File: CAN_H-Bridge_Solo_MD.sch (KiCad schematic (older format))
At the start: 49 parts, among them IC1 SI8650AB-B-IS1, IC2 A3921KLPTR-T, IC3 AP7381-50SA-7, J2 Conn_01x03, J3 Conthrough, J4 Bus_mechaken_PCIexpress_x16_1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, M1 Motor_DC, Q1 IRFB3806PBF, Q2 IRFB3806PBF, Q3 IRFB3806PBF, Q4 IRFB3806PBF, U1 LDL1117S33R_SOT223-4, U2 STM32F042K6Tx, U3 MCP2562-E-SN, U4 LDL1117S33TR_SOT223-4

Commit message: change
反転前
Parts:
- removed C14: 2.2u, Capacitor_SMD:C_0805_2012Metric_Pad1.15x1.40mm_HandSolder, symbol Device:C
- removed C15: 1u, Capacitor_SMD:C_0805_2012Metric_Pad1.15x1.40mm_HandSolder, symbol Device:C
- removed IC3: AP7381-50SA-7, SamacSys_Parts:SOT96P240X105-3N, symbol CAN_H-Bridge_Solo_MD-rescue:AP7381-50SA-7-SamacSys_Parts
- removed Q1, Q2, Q3, Q4: IRFB3806PBF, Package_TO_SOT_THT:TO-220-3_Vertical, symbol Transistor_FET:IRLB8721PBF
- added Q1, Q2, Q3, Q4: TK6R7P06PLRQ, Package_TO_SOT_SMD:TO-252-2, symbol Device:Q_NMOS_GDS
- C7: renamed from C13; value 4.7uF -> 1uF
- S1: value IKD0403101 -> DIPSW; footprint SamacSys_Parts:SOP254P980X370-8N -> Package_DIP:DIP-8_W7.62mm; symbol SamacSys_Parts:IKD0403101 -> Switch:SW_DIP_x04; Description 4 Way Surface Mount DIP Switch SPST, Raised Actuator Slide 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 -> (none)
- U1: symbol H-Bridge-MD-rescue:LD1117S33TR_SOT223-Regulator_Linear -> Regulator_Linear:LD1117S33TR_SOT223
- U2: value STM32F042K6Tx -> STM32F303K8
- U3: renamed from U4; value LDL1117S33TR_SOT223-4 -> MCP1799T-3302H/TT; footprint Package_TO_SOT_SMD:SOT-223-3_TabPin2 -> Package_TO_SOT_SMD:SOT-23; symbol H-Bridge-MD-rescue:LD1117S33TR_SOT223-Regulator_Linear -> Regulator_Linear:MCP1700-3302E_SOT23
- renumbered C3 to C1, C7 to C10, C6 to C11, C8 to C12, C12 to C13, C9 to C14, C10 to C15, C1 to C2, C2 to C3, C11 to C6, C5 to C8, C4 to C9, D6 to D1, D1 to D2, D2 to D3, D3 to D4, D4 to D5, D5 to D6, IC1 to IC2, IC2 to IC3, J2 to J1, J3 to J2, J4 to J3, R5 to R1, R8 to R10, R4 to R11, R9 to R12, R1 to R2, R2 to R3, R10 to R4, R11 to R5, R12 to R6, R6 to R7, R7 to R8, R3 to R9, U3 to U4
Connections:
- net labels added: IC_3V3
- net labels removed: +3.3V
- wire segments 114 -> 107
- no-connect marks 20 -> 19

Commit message: change
FET反転
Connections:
- net SA_0: now also M1.1 (+); no longer M1.2 (-)
- net SB_0: now also M1.2 (-); no longer M1.1 (+)
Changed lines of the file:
@@
 L Motor:Motor_DC M1
 U 1 1 5E054D53
-P 3550 6700
-F 0 "M1" V 3845 6650 50  0000 C CNN
-F 1 "Motor_DC" V 3754 6650 50  0000 C CNN
-F 2 "XT60:XT60PW" H 3550 6610 50  0001 C CNN
-F 3 "~" H 3550 6610 50  0001 C CNN
-	1    3550 6700
-	0    1    1    0
+P 3450 6700
+F 0 "M1" V 3745 6650 50  0000 C CNN
+F 1 "Motor_DC" V 3654 6650 50  0000 C CNN
+F 2 "XT60:XT60PW" H 3450 6610 50  0001 C CNN
+F 3 "~" H 3450 6610 50  0001 C CNN
+	1    3450 6700
+	0    -1   -1   0
 $EndComp
 Wire Wire Line

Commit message: change
ビアなどの増加
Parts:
- IC2: symbol SamacSys_Parts:SI8650AB-B-IS1 -> CAN_H-Bridge_Solo_MD-rescue:SI8650AB-B-IS1-SamacSys_Parts
- IC3: symbol SamacSys_Parts:A3921KLPTR-T -> CAN_H-Bridge_Solo_MD-rescue:A3921KLPTR-T-SamacSys_Parts
- U1: value LDL1117S33R_SOT223-4 -> AP2210N-3.3TRG1; footprint Package_TO_SOT_SMD:SOT-223-3_TabPin2 -> Package_TO_SOT_SMD:SOT-23
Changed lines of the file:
@@
 NoConn ~ 7800 5750
 $Comp
-L SamacSys_Parts:A3921KLPTR-T IC3
+L CAN_H-Bridge_Solo_MD-rescue:A3921KLPTR-T-SamacSys_Parts IC3
 U 1 1 5DC023BF
 P 7800 4450
@@
 Wire Wire Line
 	5450 3000 5450 3300
-$Comp
-L Regulator_Linear:LD1117S33TR_SOT223 U1
-U 1 1 5DEBD597
-P 1350 1950
-F 0 "U1" H 1200 2075 50  0000 C CNN
-F 1 "LDL1117S33R_SOT223-4" H 1350 2075 50  0000 L CNN
-F 2 "Package_TO_SOT_SMD:SOT-223-3_TabPin2" H 1350 2150 50  0001 C CNN
-F 3 "http://www.st.com/st-web-ui/static/active/en/resource/technical/document/datasheet/CD00000544.pdf" H 1450 1700 50  0001 C CNN
-	1    1350 1950
-	1    0    0    -1
-$EndComp
 $Comp
 L power:+5V #PWR01
@@
 IC_3V3
 $Comp
-L SamacSys_Parts:SI8650AB-B-IS1 IC2
+L CAN_H-Bridge_Solo_MD-rescue:SI8650AB-B-IS1-SamacSys_Parts IC2
 U 1 1 5DC0259A
 P 7250 3050
@@
 Wire Wire Line
 	5900 1350 5900 1450
+$Comp
+L Regulator_Linear:LD1117S33TR_SOT223 U1
+U 1 1 5DEBD597
+P 1350 1950
+F 0 "U1" H 1200 2075 50  0000 C CNN
+F 1 "AP2210N-3.3TRG1" H 1350 2075 50  0000 L CNN
+F 2 "Package_TO_SOT_SMD:SOT-23" H 1350 2150 50  0001 C CNN
+F 3 "" H 1450 1700 50  0001 C CNN
+	1    1350 1950
+	1    0    0    -1
+$EndComp
 $EndSCHEMATC

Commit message: Release
Release Prototype-2.0
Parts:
- C1, C13, C14, C8, C9: value 0.1uF -> 0.1u
- C10, C11, C12: value 4.7uF -> 4.7u
- C15: value 0.47uF -> 0.47u
- C2, C6, C7: value 1uF -> 1u
- C3: value 4.7uF -> 2.2u
- IC2: footprint SamacSys_Parts:SOIC127P600X175-16N -> Package_SO:SOIC-16_3.9x9.9mm_P1.27mm; symbol CAN_H-Bridge_Solo_MD-rescue:SI8650AB-B-IS1-SamacSys_Parts -> SamacSys_Parts:SI8650AB-B-IS1
- IC3: symbol CAN_H-Bridge_Solo_MD-rescue:A3921KLPTR-T-SamacSys_Parts -> SamacSys_Parts:A3921KLPTR-T
- R10, R11, R12, R9: value 21 -> 30
- U1: footprint Package_TO_SOT_SMD:SOT-23 -> Package_TO_SOT_SMD:SOT-23W_Handsoldering
- U3: footprint Package_TO_SOT_SMD:SOT-23 -> Package_TO_SOT_SMD:SOT-23_Handsoldering
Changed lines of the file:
@@
 P 9900 5400
 F 0 "C13" H 10015 5446 50  0000 L CNN
-F 1 "0.1uF" H 10015 5355 50  0000 L CNN
+F 1 "0.1u" H 10015 5355 50  0000 L CNN
 F 2 "Capacitor_SMD:C_0805_2012Metric_Pad1.15x1.40mm_HandSolder" H 9938 5250 50  0001 C CNN
 F 3 "~" H 9900 5400 50  0001 C CNN
@@
 P 7450 5800
 F 0 "C14" H 7565 5846 50  0000 L CNN
-F 1 "0.1uF" H 7565 5755 50  0000 L CNN
+F 1 "0.1u" H 7565 5755 50  0000 L CNN
 F 2 "Capacitor_SMD:C_0805_2012Metric_Pad1.15x1.40mm_HandSolder" H 7488 5650 50  0001 C CNN
 F 3 "~" H 7450 5800 50  0001 C CNN
@@
 NoConn ~ 7800 5750
 $Comp
-L CAN_H-Bridge_Solo_MD-rescue:A3921KLPTR-T-SamacSys_Parts IC3
+L SamacSys_Parts:A3921KLPTR-T IC3
 U 1 1 5DC023BF
 P 7800 4450
@@
 P 5900 3950
 F 0 "C8" V 5648 3950 50  0000 C CNN
-F 1 "0.1uF" V 5739 3950 50  0000 C CNN
+F 1 "0.1u" V 5739 3950 50  0000 C CNN
 F 2 "Capacitor_SMD:C_0805_2012Metric_Pad1.15x1.40mm_HandSolder" H 5938 3800 50  0001 C CNN
 F 3 "~" H 5900 3950 50  0001 C CNN
@@
 P 4500 4600
 F 0 "C9" V 4248 4600 50  0000 C CNN
-F 1 "0.1uF" V 4339 4600 50  0000 C CNN
+F 1 "0.1u" V 4339 4600 50  0000 C CNN
 F 2 "Capacitor_SMD:C_0805_2012Metric_Pad1.15x1.40mm_HandSolder" H 4538 4450 50  0001 C CNN
 F 3 "~" H 4500 4600 50  0001 C CNN
@@
 P 1000 2100
 F 0 "C2" V 748 2100 50  0000 C CNN
-F 1 "1uF" V 839 2100 50  0000 C CNN
+F 1 "1u" V 839 2100 50  0000 C CNN
 F 2 "Capacitor_SMD:C_0805_2012Metric_Pad1.15x1.40mm_HandSolder" H 1038 1950 50  0001 C CNN
 F 3 "~" H 1000 2100 50  0001 C CNN
@@
 P 1700 2100
 F 0 "C3" V 1448 2100 50  0000 C CNN
-F 1 "4.7uF" V 1539 2100 50  0000 C CNN
+F 1 "2.2u" V 1539 2100 50  0000 C CNN
 F 2 "Capacitor_SMD:C_0805_2012Metric_Pad1.15x1.40mm_HandSolder" H 1738 1950 50  0001 C CNN
 F 3 "~" H 1700 2100 50  0001 C CNN
@@
 P 4100 1150
 F 0 "C1" V 3848 1150 50  0000 C CNN
-F 1 "0.1uF" V 3939 1150 50  0000 C CNN
+F 1 "0.1u" V 3939 1150 50  0000 C CNN
 F 2 "Capacitor_SMD:C_0805_2012Metric_Pad1.15x1.40mm_HandSolder" H 4138 1000 50  0001 C CNN
 F 3 "~" H 4100 1150 50  0001 C CNN
@@
 P 7150 4900
 F 0 "C10" H 7264 4854 50  0000 L CNN
-F 1 "4.7uF" H 7264 4945 50  0000 L CNN
+F 1 "4.7u" H 7264 4945 50  0000 L CNN
 F 2 "Capacitor_SMD:C_0805_2012Metric_Pad1.15x1.40mm_HandSolder" H 7188 4750 50  0001 C CNN
 F 3 "~" H 7150 4900 50  0001 C CNN
@@
 P 7150 5400
 F 0 "C12" H 6823 5446 50  0000 L CNN
-F 1 "4.7uF" H 6823 5355 50  0000 L CNN
+F 1 "4.7u" H 6823 5355 50  0000 L CNN
 F 2 "Capacitor_SMD:C_0805_2012Metric_Pad1.15x1.40mm_HandSolder" H 7188 5250 50  0001 C CNN
 F 3 "~" H 7150 5400 50  0001 C CNN
@@
 P 9450 5800
 F 0 "C15" H 9074 5754 50  0000 L CNN
-F 1 "0.47uF" H 9074 5845 50  0000 L CNN
+F 1 "0.47u" H 9074 5845 50  0000 L CNN
 F 2 "Capacitor_SMD:C_0805_2012Metric_Pad1.15x1.40mm_HandSolder" H 9488 5650 50  0001 C CNN
 F 3 "~" H 9450 5800 50  0001 C CNN
@@
 P 6300 5000
 F 0 "C11" H 6415 5046 50  0000 L CNN
-F 1 "4.7uF" H 6415 4955 50  0000 L CNN
+F 1 "4.7u" H 6415 4955 50  0000 L CNN
 F 2 "Capacitor_SMD:C_0805_2012Metric_Pad1.15x1.40mm_HandSolder" H 6338 4850 50  0001 C CNN
 F 3 "~" H 6300 5000 50  0001 C CNN
@@
 P 9900 3150
 F 0 "C6" V 9648 3150 50  0000 C CNN
-F 1 "1uF" V 9739 3150 50  0000 C CNN
+F 1 "1u" V 9739 3150 50  0000 C CNN
 F 2 "Capacitor_SMD:C_0805_2012Metric_Pad1.15x1.40mm_HandSolder" H 9938 3000 50  0001 C CNN
 F 3 "~" H 9900 3150 50  0001 C CNN
@@
 P 10600 3150
 F 0 "C7" V 10348 3150 50  0000 C CNN
-F 1 "1uF" V 10439 3150 50  0000 C CNN
+F 1 "1u" V 10439 3150 50  0000 C CNN
 F 2 "Capacitor_SMD:C_0805_2012Metric_Pad1.15x1.40mm_HandSolder" H 10638 3000 50  0001 C CNN
 F 3 "~" H 10600 3150 50  0001 C CNN
@@
 F 0 "U3" H 10100 3125 50  0000 C CNN
 F 1 "MCP1799T-3302H/TT" H 10250 3125 50  0000 L CNN
-F 2 "Package_TO_SOT_SMD:SOT-23" H 10250 3200 50  0001 C CNN
+F 2 "Package_TO_SOT_SMD:SOT-23_Handsoldering" H 10250 3200 50  0001 C CNN
 F 3 "" H 10350 2750 50  0001 C CNN
 	1    10250 3000
@@
 P 4700 7050
 F 0 "R12" V 4815 6975 50  0000 L CNN
-F 1 "21" V 4906 6975 50  0000 L CNN
+F 1 "30" V 4906 6975 50  0000 L CNN
 F 2 "Resistor_SMD:R_0603_1608Metric_Pad1.05x0.95mm_HandSolder" V 4630 7050 50  0001 C CNN
 F 3 "~" H 4700 7050 50  0001 C CNN
@@
 P 2350 6350
 F 0 "R9" V 2550 6275 50  0000 L CNN
-F 1 "21" V 2450 6275 50  0000 L CNN
+F 1 "30" V 2450 6275 50  0000 L CNN
 F 2 "Resistor_SMD:R_0603_1608Metric_Pad1.05x0.95mm_HandSolder" V 2280 6350 50  0001 C CNN
 F 3 "~" H 2350 6350 50  0001 C CNN
@@
 P 2350 7050
 F 0 "R11" V 2550 6974 50  0000 L CNN
-F 1 "21" V 2450 6974 50  0000 L CNN
+F 1 "30" V 2450 6974 50  0000 L CNN
 F 2 "Resistor_SMD:R_0603_1608Metric_Pad1.05x0.95mm_HandSolder" V 2280 7050 50  0001 C CNN
 F 3 "~" H 2350 7050 50  0001 C CNN
@@
 P 4700 6350
 F 0 "R10" V 4815 6276 50  0000 L CNN
-F 1 "21" V 4906 6276 50  0000 L CNN
+F 1 "30" V 4906 6276 50  0000 L CNN
 F 2 "Resistor_SMD:R_0603_1608Metric_Pad1.05x0.95mm_HandSolder" V 4630 6350 50  0001 C CNN
 F 3 "~" H 4700 6350 50  0001 C CNN
@@
 IC_3V3
 $Comp
-L CAN_H-Bridge_Solo_MD-rescue:SI8650AB-B-IS1-SamacSys_Parts IC2
+L SamacSys_Parts:SI8650AB-B-IS1 IC2
 U 1 1 5DC0259A
 P 7250 3050
 F 0 "IC2" H 7473 3315 50  0000 L CNN
 F 1 "SI8650AB-B-IS1" H 7473 3224 50  0000 L CNN
-F 2 "SamacSys_Parts:SOIC127P600X175-16N" H 8200 3150 50  0001 L CNN
+F 2 "Package_SO:SOIC-16_3.9x9.9mm_P1.27mm" H 8200 3150 50  0001 L CNN
 F 3 "https://componentsearchengine.com/Datasheets/1/SI8651BB-B-IS1.pdf" H 8200 3050 50  0001 L CNN
 F 4 "Isolator, Si8650AB-B-IS1 Silicon Labs Si8650AB-B-IS1 PCB SMT 5-channel Digital Isolator, 2.5 kV, 16-Pin SOIC" H 8200 2950 50  0001 L CNN "Description"
@@
 F 0 "U1" H 1200 2075 50  0000 C CNN
 F 1 "AP2210N-3.3TRG1" H 1350 2075 50  0000 L CNN
-F 2 "Package_TO_SOT_SMD:SOT-23" H 1350 2150 50  0001 C CNN
+F 2 "Package_TO_SOT_SMD:SOT-23W_Handsoldering" H 1350 2150 50  0001 C CNN
 F 3 "" H 1450 1700 50  0001 C CNN
 	1    1350 1950

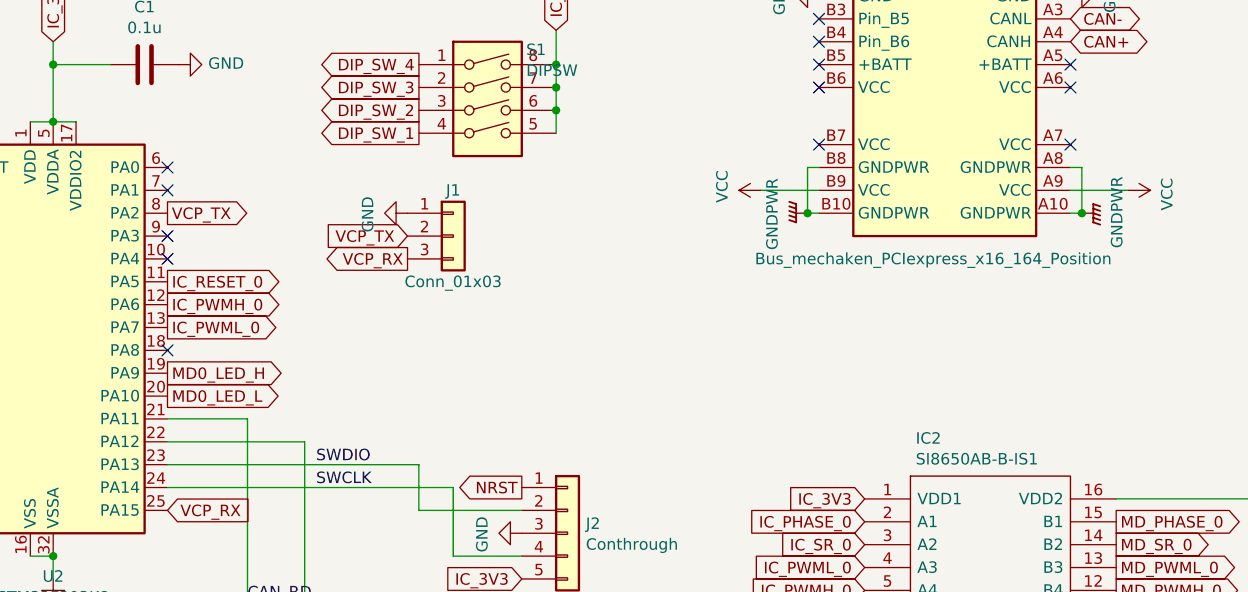
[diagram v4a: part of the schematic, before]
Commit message: Update: エンコーダ対応
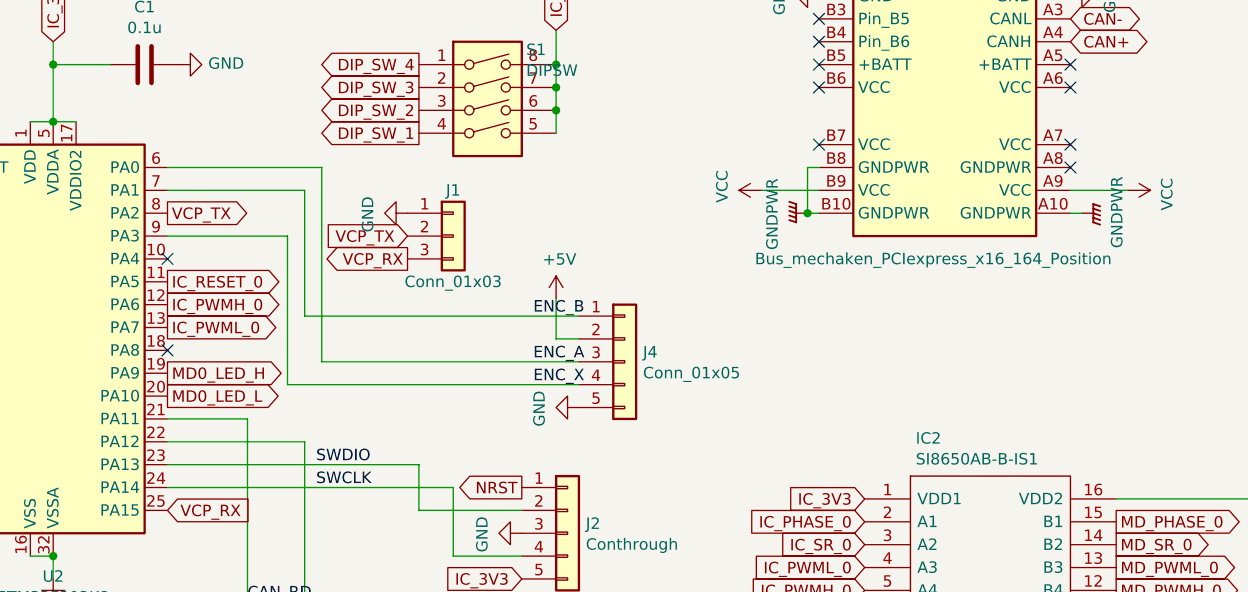
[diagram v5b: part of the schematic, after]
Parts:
- added J4: Conn_01x05, Connector_PinHeader_2.54mm:PinHeader_1x05_P2.54mm_Vertical, symbol Connector_Generic:Conn_01x05
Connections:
- net +5V: now also J4.2 (Pin_2)
- net GND: now also J4.5 (Pin_5)
- net GNDPWR: no longer J3.A8 (GNDPWR)
- net ENC_A: now reaches U2.6 (PA0)
- net ENC_A: now also J4.3 (Pin_3)
- net ENC_B: now reaches U2.7 (PA1)
- net ENC_B: now also J4.1 (Pin_1)
- net ENC_X: now reaches U2.9 (PA3)
- net ENC_X: now also J4.4 (Pin_4)
- no-connect marks 19 -> 17
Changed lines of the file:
@@
 $EndComp
-Wire Wire Line
-	7050 1600 7000 1600
-Wire Wire Line
-	7000 1600 7000 1800
 Wire Wire Line
 	7000 1800 7050 1800
-Connection ~ 7000 1800
 Wire Wire Line
 	7050 1700 6800 1700
 Wire Wire Line
-	8150 1600 8200 1600
-Wire Wire Line
 	8150 1800 8200 1800
 Wire Wire Line
 	8400 1700 8150 1700
-Wire Wire Line
-	8200 1600 8200 1800
-Connection ~ 8200 1800
 NoConn ~ 3200 2100
 NoConn ~ 3200 2200
-NoConn ~ 4200 1600
-NoConn ~ 4200 1700
-NoConn ~ 4200 1900
 NoConn ~ 4200 2000
 NoConn ~ 4200 2400
@@
 	1    0    0    -1
 $EndComp
+$Comp
+L Connector_Generic:Conn_01x05 J4
+U 1 1 602E5899
+P 6200 2450
+F 0 "J4" H 6280 2492 50  0000 L CNN
+F 1 "Conn_01x05" H 6280 2401 50  0000 L CNN
+F 2 "Connector_PinHeader_2.54mm:PinHeader_1x05_P2.54mm_Vertical" H 6200 2450 50  0001 C CNN
+F 3 "~" H 6200 2450 50  0001 C CNN
+	1    6200 2450
+	1    0    0    -1
+$EndComp
+$Comp
+L power:GND #PWR0102
+U 1 1 602E8414
+P 6000 2650
+F 0 "#PWR0102" H 6000 2400 50  0001 C CNN
+F 1 "GND" H 6005 2477 50  0000 C CNN
+F 2 "" H 6000 2650 50  0001 C CNN
+F 3 "" H 6000 2650 50  0001 C CNN
+	1    6000 2650
+	0    1    1    0
+$EndComp
+$Comp
+L power:+5V #PWR0103
+U 1 1 6031EF32
+P 5900 2175
+F 0 "#PWR0103" H 5900 2025 50  0001 C CNN
+F 1 "+5V" H 5915 2348 50  0000 C CNN
+F 2 "" H 5900 2175 50  0001 C CNN
+F 3 "" H 5900 2175 50  0001 C CNN
+	1    5900 2175
+	1    0    0    -1
+$EndComp
+Wire Wire Line
+	5900 2175 5900 2350
+Wire Wire Line
+	5900 2350 6000 2350
+Wire Wire Line
+	4875 1600 4200 1600
+Wire Wire Line
+	4800 1700 4200 1700
+Wire Wire Line
+	4725 2550 4725 1900
+Wire Wire Line
+	4725 1900 4200 1900
+Wire Wire Line
+	4725 2550 6000 2550
+Text Label 5800 2250 0    50   ~ 0
+ENC_B
+Text Label 5800 2450 0    50   ~ 0
+ENC_A
+Text Label 5800 2550 0    50   ~ 0
+ENC_X
+Wire Wire Line
+	4800 1700 4800 2250
+Wire Wire Line
+	4800 2250 6000 2250
+Wire Wire Line
+	4875 1600 4875 2450
+Wire Wire Line
+	4875 2450 6000 2450
+Connection ~ 7000 1800
+Wire Wire Line
+	7000 1600 7000 1800
+Wire Wire Line
+	7050 1600 7000 1600
+NoConn ~ 8150 1600
 $EndSCHEMATC

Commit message: Update: MCUをF042K6からF303K8へ変更
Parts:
- U2: symbol MCU_ST_STM32F0:STM32F042K6Tx -> MCU_ST_STM32F3:STM32F303K8Tx
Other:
- moved on the sheet: R1, U2
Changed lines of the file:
@@
 	-1   0    0    1
 $EndComp
-Text GLabel 3200 1600 0    50   Input ~ 0
+Text GLabel 3100 1600 0    50   Input ~ 0
 NRST
 Text GLabel 4200 3100 2    50   Input ~ 0
@@
 L Device:R R1
 U 1 1 5D5AB267
-P 2650 3100
-F 0 "R1" V 2443 3100 50  0000 C CNN
-F 1 "10k" V 2534 3100 50  0000 C CNN
-F 2 "Resistor_SMD:R_0603_1608Metric_Pad1.05x0.95mm_HandSolder" V 2580 3100 50  0001 C CNN
-F 3 "~" H 2650 3100 50  0001 C CNN
-	1    2650 3100
+P 2550 1800
+F 0 "R1" V 2343 1800 50  0000 C CNN
+F 1 "10k" V 2434 1800 50  0000 C CNN
+F 2 "Resistor_SMD:R_0603_1608Metric_Pad1.05x0.95mm_HandSolder" V 2480 1800 50  0001 C CNN
+F 3 "~" H 2550 1800 50  0001 C CNN
+	1    2550 1800
 	0    1    1    0
 $EndComp
@@
 Wire Wire Line
 	9200 5550 9900 5550
-Text GLabel 3200 2500 0    50   Output ~ 0
+Text GLabel 3100 2600 0    50   Output ~ 0
 IC_PHASE_0
-Text GLabel 3200 2400 0    50   Output ~ 0
+Text GLabel 3100 2500 0    50   Output ~ 0
 IC_SR_0
 Text GLabel 4200 2100 2    50   Output ~ 0
@@
 Text Label 4550 3500 0    50   ~ 0
 CAN_RD
-Text Label 2850 3100 0    50   ~ 0
+Text Label 2750 1800 0    50   ~ 0
 BOOT
 $Comp
@@
 Text GLabel 5300 1150 0    50   Output ~ 0
 DIP_SW_4
-Text GLabel 3200 2900 0    50   Input ~ 0
+Text GLabel 3100 3000 0    50   Input ~ 0
 DIP_SW_4
-Text GLabel 3200 2800 0    50   Input ~ 0
+Text GLabel 3100 2900 0    50   Input ~ 0
 DIP_SW_3
-Text GLabel 3200 2700 0    50   Input ~ 0
+Text GLabel 3100 2800 0    50   Input ~ 0
 DIP_SW_2
 Wire Wire Line
@@
 Connection ~ 3700 3300
 Wire Wire Line
-	3200 3100 2800 3100
-$Comp
-L MCU_ST_STM32F0:STM32F042K6Tx U2
+	3100 1800 2700 1800
+$Comp
+L MCU_ST_STM32F3:STM32F303K8Tx U2
 U 1 1 5DA7A10A
 P 3700 2300
@@
 F 1 "STM32F303K8" H 3700 1120 50  0000 C CNN
 F 2 "Package_QFP:LQFP-32_7x7mm_P0.8mm" H 3300 1400 50  0001 R CNN
-F 3 "http://www.st.com/st-web-ui/static/active/en/resource/technical/document/datasheet/DM00105814.pdf" H 3700 2300 50  0001 C CNN
+F 3 "http://www.st.com/st-web-ui/static/active/en/resource/technical/document/datasheet/DM00092070.pdf" H 3700 2300 50  0001 C CNN
 	1    3700 2300
 	1    0    0    -1
 $EndComp
-Text GLabel 3200 2600 0    50   Input ~ 0
+Text GLabel 3100 2700 0    50   Input ~ 0
 DIP_SW_1
 Wire Wire Line
@@
 Wire Wire Line
 	8400 1700 8150 1700
-NoConn ~ 3200 2100
-NoConn ~ 3200 2200
 NoConn ~ 4200 2000
 NoConn ~ 4200 2400
-NoConn ~ 3200 3000
 Text GLabel 10700 5250 2    50   Input ~ 0
 V5
@@
 L power:GND #PWR024
 U 1 1 5D5AAC2B
-P 2500 3100
-F 0 "#PWR024" H 2500 2850 50  0001 C CNN
-F 1 "GND" H 2505 2927 50  0000 C CNN
-F 2 "" H 2500 3100 50  0001 C CNN
-F 3 "" H 2500 3100 50  0001 C CNN
-	1    2500 3100
+P 2400 1800
+F 0 "#PWR024" H 2400 1550 50  0001 C CNN
+F 1 "GND" H 2405 1627 50  0000 C CNN
+F 2 "" H 2400 1800 50  0001 C CNN
+F 3 "" H 2400 1800 50  0001 C CNN
+	1    2400 1800
 	1    0    0    -1
 $EndComp
@@
 	7050 1600 7000 1600
 NoConn ~ 8150 1600
+NoConn ~ 3100 2200
+NoConn ~ 3100 2300
+NoConn ~ 3100 3100
 $EndSCHEMATC
